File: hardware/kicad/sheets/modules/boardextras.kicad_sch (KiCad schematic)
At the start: 1 part

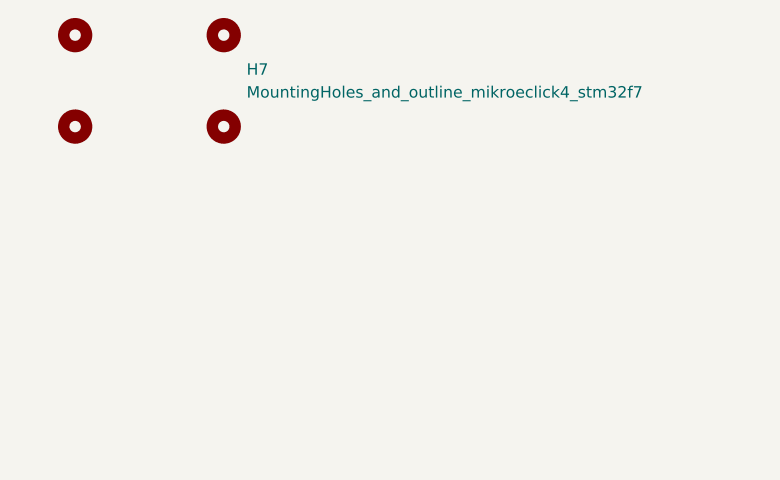
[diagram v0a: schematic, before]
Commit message: sheet optimized ports and current sensor
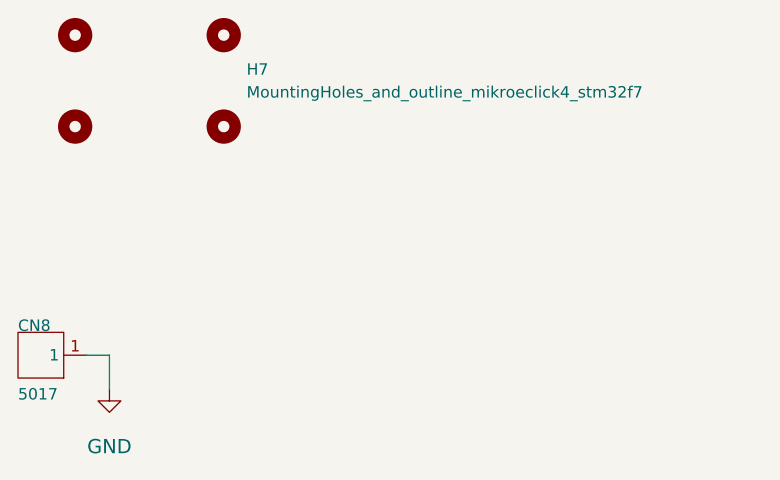
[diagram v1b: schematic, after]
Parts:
- added CN8: 5017, 5v rail sm-easyedapro:CONN-SMD_5017, symbol 5v rail sm-easyedapro:5017_C9900015874
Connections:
- new net GND: CN8.1
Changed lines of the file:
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@@
 	(generator_version "9.0")
 	(paper "A4")
+	(wire
+		(pts
+			(xy 83.82 125.73) (xy 83.82 129.54)
+		)
+		(stroke
+			(width 0)
+			(type default)
+		)
+	)
+	(wire
+		(pts
+			(xy 81.28 125.73) (xy 83.82 125.73)
+		)
+		(stroke
+			(width 0)
+			(type default)
+		)
+	)
+	(symbol
+		(lib_id "5v rail sm-easyedapro:5017_C9900015874")
+		(at 76.2 125.73 180)
+		(unit 1)
+		(exclude_from_sim no)
+		(in_bom yes)
+		(on_board yes)
+		(dnp no)
+		(property "Reference" "CN8"
+			(at 73.66 123.19 0)
+			(effects
+				(font
+					(size 1.27 1.27)
+				)
+				(justify right top)
+			)
+		)
+		(property "Value" "5017"
+			(at 73.66 130.81 0)
+			(effects
+				(font
+					(size 1.27 1.27)
+				)
+				(justify right top)
+			)
+		)
+		(property "Footprint" "5v rail sm-easyedapro:CONN-SMD_5017"
+			(at 76.2 125.73 0)
+			(effects
+				(font
+					(size 1.27 1.27)
+				)
+				(hide yes)
+			)
+		)
+		(property "Datasheet" ""
+			(at 76.2 125.73 0)
+			(effects
+				(font
+					(size 1.27 1.27)
+				)
+				(hide yes)
+			)
+		)
+		(property "Description" ""
+			(at 76.2 125.73 0)
+			(effects
+				(font
+					(size 1.27 1.27)
+				)
+				(hide yes)
+			)
+		)
+		(property "Manufacturer Part" "5017"
+			(at 76.2 125.73 0)
+			(effects
+				(font
+					(size 1.27 1.27)
+				)
+				(hide yes)
+			)
+		)
+		(property "Supplier Part" "C9900015874"
+			(at 76.2 125.73 0)
+			(effects
+				(font
+					(size 1.27 1.27)
+				)
+				(hide yes)
+			)
+		)
+		(property "Supplier" "LCSC"
+			(at 76.2 125.73 0)
+			(effects
+				(font
+					(size 1.27 1.27)
+				)
+				(hide yes)
+			)
+		)
+		(property "LCSC Part Name" "5017"
+			(at 76.2 125.73 0)
+			(effects
+				(font
+					(size 1.27 1.27)
+				)
+				(hide yes)
+			)
+		)
+		(pin "1"
+		)
+		(instances
+			(project "svea_powerboard_rev3"
+				(path "/3f85abf4-0b95-4c4a-b7e9-06f59ca1ea3d/ed916956-09ce-4402-8cd6-0b33381a1896"
+					(reference "CN8")
+					(unit 1)
+				)
+			)
+		)
+	)
+	(symbol
+		(lib_id "power:GND")
+		(at 83.82 129.54 0)
+		(unit 1)
+		(exclude_from_sim no)
+		(in_bom yes)
+		(on_board yes)
+		(dnp no)
+		(property "Reference" "#PWR034"
+			(at 83.82 129.54 0)
+			(effects
+				(font
+					(size 1.27 1.27)
+				)
+				(hide yes)
+			)
+		)
+		(property "Value" "GND"
+			(at 83.82 135.89 0)
+			(effects
+				(font
+					(size 1.5748 1.5748)
+				)
+			)
+		)
+		(property "Footprint" ""
+			(at 83.82 129.54 0)
+			(effects
+				(font
+					(size 1.27 1.27)
+				)
+				(hide yes)
+			)
+		)
+		(property "Datasheet" ""
+			(at 83.82 129.54 0)
+			(effects
+				(font
+					(size 1.27 1.27)
+				)
+				(hide yes)
+			)
+		)
+		(property "Description" ""
+			(at 83.82 129.54 0)
+			(effects
+				(font
+					(size 1.27 1.27)
+				)
+				(hide yes)
+			)
+		)
+		(pin "1"
+		)
+		(instances
+			(project "svea_powerboard_rev3"
+				(path "/3f85abf4-0b95-4c4a-b7e9-06f59ca1ea3d/ed916956-09ce-4402-8cd6-0b33381a1896"
+					(reference "#PWR034")
+					(unit 1)
+				)
+			)
+		)
+	)
 	(symbol
 		(lib_id "5v rail sm-easyedapro:MountingHoles_and_outline_mikroeclick4_stm32f7")

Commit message: resheeted bms and fixed links for the 12v buck
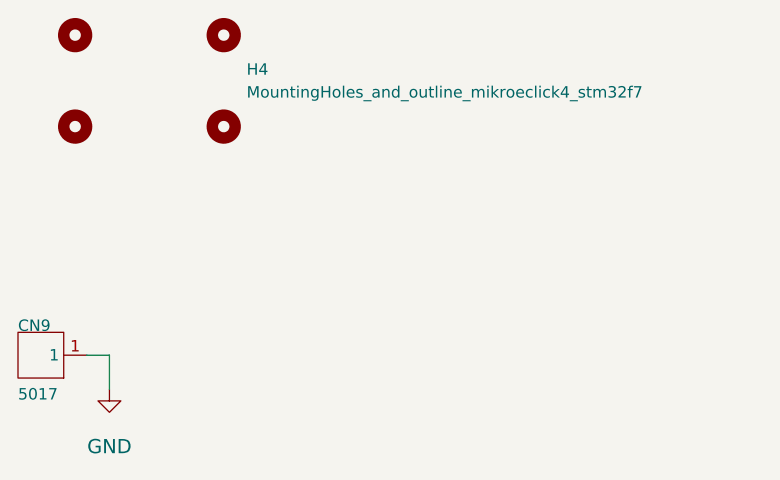
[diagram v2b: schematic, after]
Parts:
- renumbered CN8 to CN9, H7 to H4
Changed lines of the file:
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@@
 		(on_board yes)
 		(dnp no)
-		(property "Reference" "CN8"
+		(property "Reference" "CN9"
 			(at 73.66 123.19 0)
 			(effects
@@
 			(project "svea_powerboard_rev3"
 				(path "/3f85abf4-0b95-4c4a-b7e9-06f59ca1ea3d/ed916956-09ce-4402-8cd6-0b33381a1896"
-					(reference "CN8")
+					(reference "CN9")
 					(unit 1)
 				)
@@
 		(on_board yes)
 		(dnp no)
-		(property "Reference" "#PWR034"
+		(property "Reference" "#PWR081"
 			(at 83.82 129.54 0)
 			(effects
@@
 			(project "svea_powerboard_rev3"
 				(path "/3f85abf4-0b95-4c4a-b7e9-06f59ca1ea3d/ed916956-09ce-4402-8cd6-0b33381a1896"
-					(reference "#PWR034")
+					(reference "#PWR081")
 					(unit 1)
 				)
@@
 		(dnp no)
 		(fields_autoplaced yes)
-		(property "Reference" "H7"
+		(property "Reference" "H4"
 			(at 99.06 93.9799 0)
 			(effects
@@
 			(project "svea_powerboard_rev3"
 				(path "/3f85abf4-0b95-4c4a-b7e9-06f59ca1ea3d/ed916956-09ce-4402-8cd6-0b33381a1896"
-					(reference "H7")
+					(reference "H4")
 					(unit 1)
 				)

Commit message: various improvements
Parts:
- renumbered CN9 to CN11, H4 to H7
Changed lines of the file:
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@@
 		(on_board yes)
 		(dnp no)
-		(property "Reference" "CN9"
+		(property "Reference" "CN11"
 			(at 73.66 123.19 0)
 			(effects
@@
 			(project "svea_powerboard_rev3"
 				(path "/3f85abf4-0b95-4c4a-b7e9-06f59ca1ea3d/ed916956-09ce-4402-8cd6-0b33381a1896"
-					(reference "CN9")
+					(reference "CN11")
 					(unit 1)
 				)
@@
 		(on_board yes)
 		(dnp no)
-		(property "Reference" "#PWR081"
+		(property "Reference" "#PWR0140"
 			(at 83.82 129.54 0)
 			(effects
@@
 			(project "svea_powerboard_rev3"
 				(path "/3f85abf4-0b95-4c4a-b7e9-06f59ca1ea3d/ed916956-09ce-4402-8cd6-0b33381a1896"
-					(reference "#PWR081")
+					(reference "#PWR0140")
 					(unit 1)
 				)
@@
 		(dnp no)
 		(fields_autoplaced yes)
-		(property "Reference" "H4"
+		(property "Reference" "H7"
 			(at 99.06 93.9799 0)
 			(effects
@@
 			(project "svea_powerboard_rev3"
 				(path "/3f85abf4-0b95-4c4a-b7e9-06f59ca1ea3d/ed916956-09ce-4402-8cd6-0b33381a1896"
-					(reference "H4")
+					(reference "H7")
 					(unit 1)
 				)

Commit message: various improvements
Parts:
- removed CN11: 5017, 5v rail sm-easyedapro:CONN-SMD_5017, symbol 5v rail sm-easyedapro:5017_C9900015874
- removed H7: MountingHoles_and_outline_mikroeclick4_stm32f7, 5v rail sm-easyedapro:stm32f7MikroeClick4Model, symbol 5v rail sm-easyedapro:MountingHoles_and_outline_mikroeclick4_stm32f7
